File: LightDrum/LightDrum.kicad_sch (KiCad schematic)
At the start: 27 parts, among them J102 JTAG, Q101 RQ5A030AP, SW101 SW_SPDT, U101 STM32F103VEH6, U102 24LC04, Y101 8MHz, Y102 32.768KHz

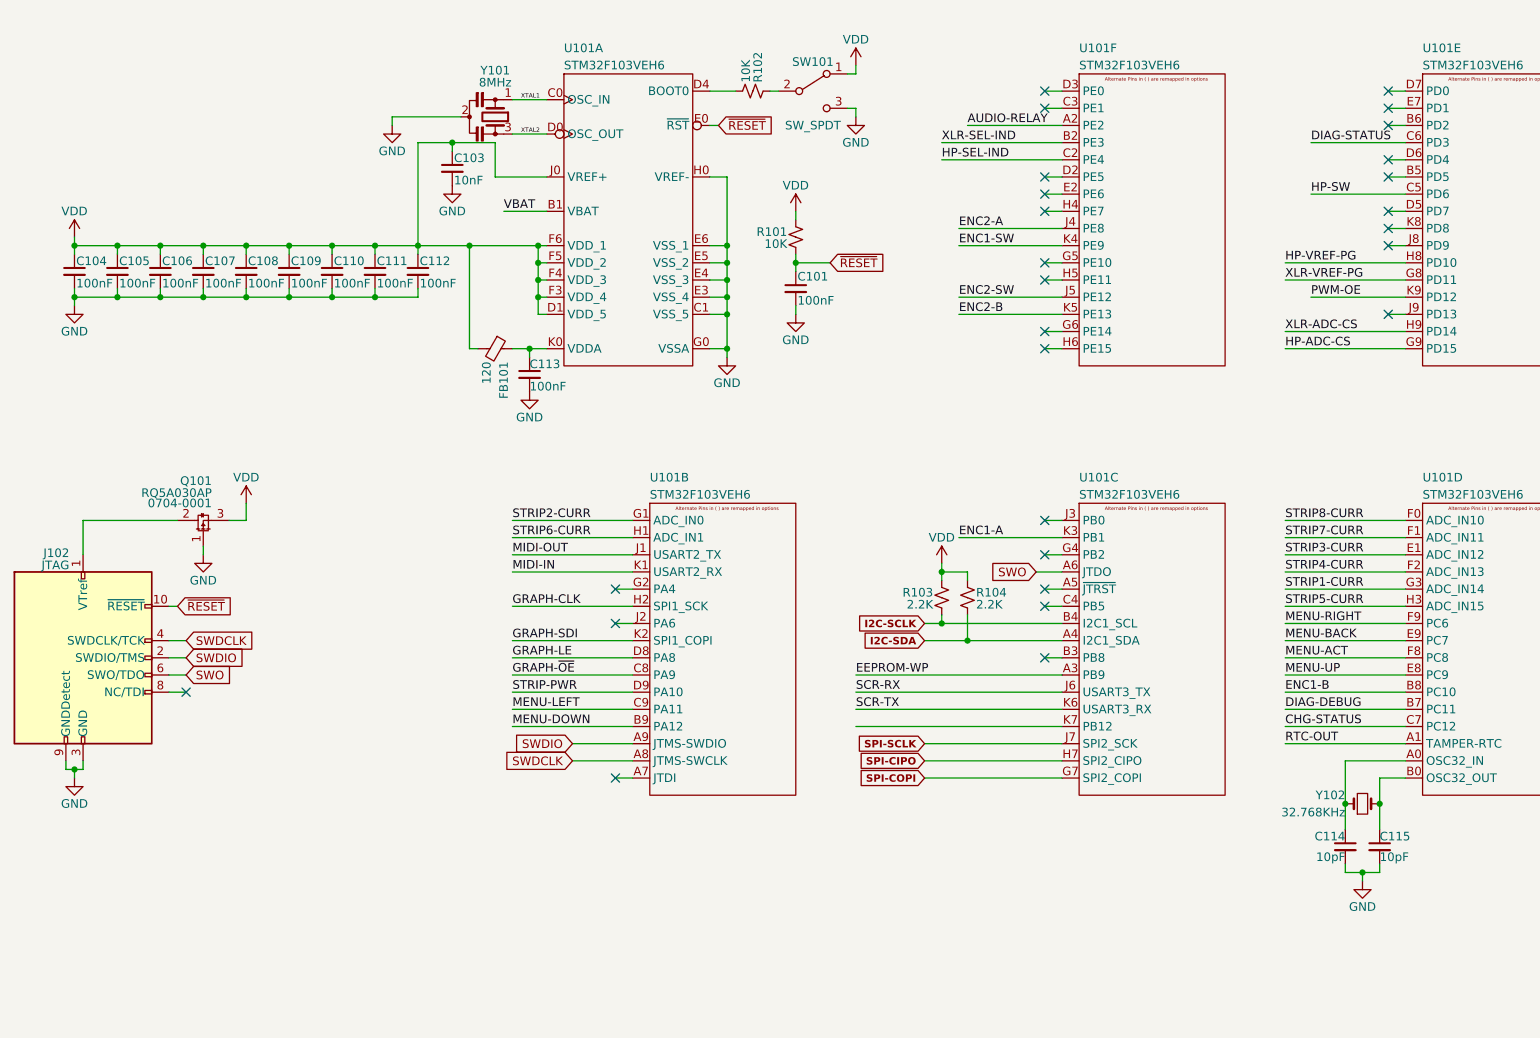
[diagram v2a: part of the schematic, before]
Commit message: Remove RTC and battery
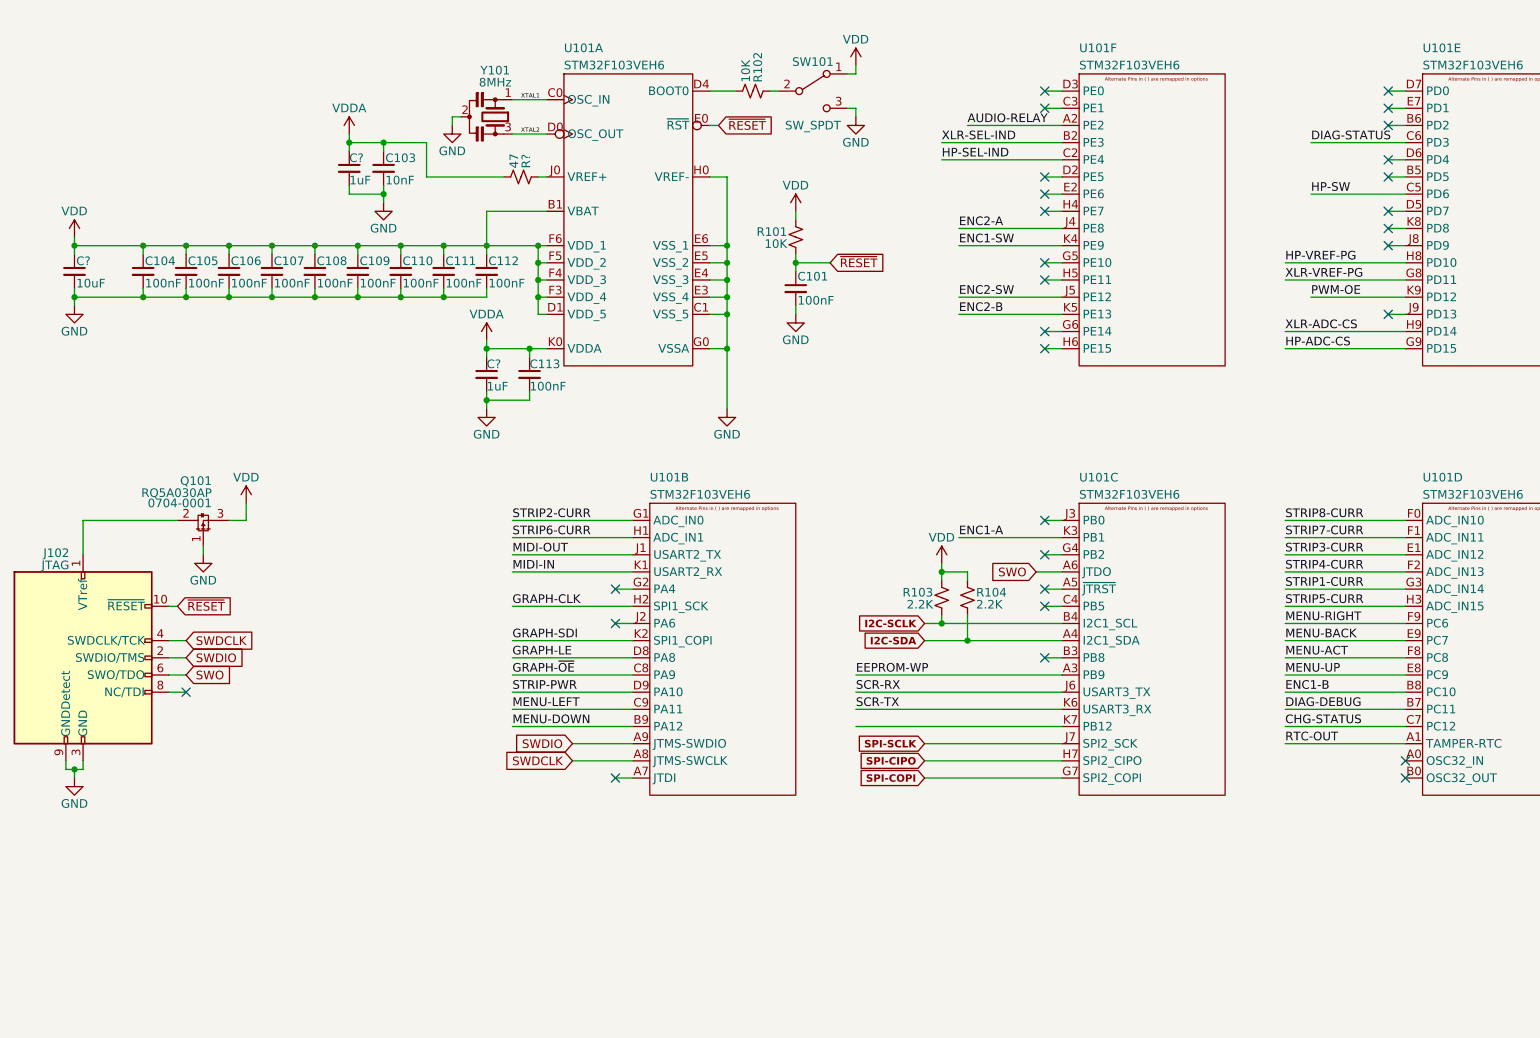
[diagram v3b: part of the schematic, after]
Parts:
- removed C114, C115: 10pF, Capacitor_SMD:C_0402_1005Metric, symbol Device:C_Small
- removed FB101: 120, Inductor_SMD:L_0603_1608Metric, symbol Device:FerriteBead_Small
- removed Y102: 32.768KHz, Crystal:Crystal_SMD_MicroCrystal_CC7V-T1A-2Pin_3.2x1.5mm, symbol Device:Crystal_Small
- added C? (x2): 1uF, Capacitor_SMD:C_0805_2012Metric, symbol Device:C_Small
- added C?: 10uF, Capacitor_SMD:C_1210_3225Metric, symbol Device:C_Small
- added R?: 47, Resistor_SMD:R_0402_1005Metric, symbol Device:R_Small_US
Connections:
- net GND: now also C?.2, C?.2, C?.2
- net VBAT: no longer U101.B1 (VBAT)
- net VDD: now also U101.B1 (VBAT), C?.1; no longer C103.1, U101.J0 (VREF+)
- net VDDA: now reaches C113.1, U101.K0 (VDDA)
- net VDDA: now also C103.1, C?.1, C?.1, R?.2
- new net: R?.1, U101.J0 (VREF+)
- no-connect marks 27 -> 29
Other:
- moved on the sheet: C103, C104, C105, C106, C107, C108, C109, C110, C111, C112

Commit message: Swap mcu again... (WIP)
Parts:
- removed C103: 10nF, Capacitor_SMD:C_0402_1005Metric, symbol Device:C_Small
- removed C104, C105, C106, C107, C108, C109, C110, C111, C112, C113: 100nF, Capacitor_SMD:C_0402_1005Metric, symbol Device:C_Small
- removed C? (x2): 1uF, Capacitor_SMD:C_0805_2012Metric, symbol Device:C_Small
- removed C?: 10uF, Capacitor_SMD:C_1210_3225Metric, symbol Device:C_Small
- removed R102: 10K, Resistor_SMD:R_0402_1005Metric, symbol Device:R_Small_US
- removed R?: 47, Resistor_SMD:R_0402_1005Metric, symbol Device:R_Small_US
- removed SW101: SW_SPDT, Daxxn_Switches:EG1218, symbol Switch:SW_SPDT
- removed U101: STM32F103VEH6, Daxxn_Packages:LFBGA-100_P0.8mm, symbol Daxxn_MicroControllers:STM32F103VEH6
- added C? (x2): 2.2uF, Capacitor_SMD:C_0805_2012Metric, symbol Device:C_Small
- added R? (x2): 10K, Resistor_SMD:R_0402_1005Metric, symbol Device:R_Small_US
- added STM101: STM32F446ZCH6, Daxxn_Packages:UFBGA144-7x7xOP6, symbol Daxxn_STMicros:STM32F446ZCH6
- added SW?: BOOT0, Daxxn_Switches:EG1218, symbol Switch:SW_SPDT
- added SW?: BOOT1, Daxxn_Switches:EG1218, symbol Switch:SW_SPDT
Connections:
- net GND: now also C?.2, C?.2, STM101.H5 (BYPASS-REG), SW?.3 (C), SW?.3 (C)
- net GRAPH-CLK: now also STM101.A3 (PE2)
- net GRAPH-SDI: now also STM101.B4 (PE6)
- net I2C-SCLK: now also STM101.C5 (PB8)
- net I2C-SDA: now also STM101.B5 (PB9)
- net MIDI-IN: now also STM101.A8 (PD6)
- net MIDI-OUT: now also STM101.B9 (PD5)
- net SCR-RX: now also STM101.D6 (PB7)
- net SCR-TX: now also STM101.C6 (PB6)
- net SPI-CIPO: now also STM101.H3 (PC2)
- net SPI-COPI: now also STM101.H2 (PC1)
- net SPI-SCLK: now also STM101.D9 (PD3)
- net STRIP1-CURR: now also STM101.J2 (PA0)
- net STRIP2-CURR: now also STM101.K2 (PA1)
- net STRIP3-CURR: now also STM101.L2 (PA2)
- net STRIP4-CURR: now also STM101.M2 (PA3)
- net STRIP5-CURR: now also STM101.J3 (PA4)
- net STRIP6-CURR: now also STM101.K3 (PA5)
- net STRIP7-CURR: now also STM101.L3 (PA6)
- net STRIP8-CURR: now also STM101.M3 (PA7)
- net SWDCLK: now also STM101.A11 (PA14/SWCLK)
- net SWDIO: now also STM101.A12 (PA13/SWDIO)
- net SWO: now also STM101.A7 (PB3/JTDO)
- net VDD: now also STM101.C2 (VBAT), STM101.E5 (PDR-ON), SW?.1 (A), SW?.1 (A)
- net XTAL1: now also STM101.D1 (OSC-IN)
- net XTAL2: now also STM101.E1 (OSC-OUT)
- net ~{RESET}: now also STM101.F1 (~{RESET})
- new net: R?.1, SW?.2 (B) (x2)
- new net: R?.2, STM101.D5 (BOOT0)
- new net: C?.1, STM101.H7 (VCAP1)
- new net: C?.1, STM101.G9 (VCAP2)
- new net BOOT1: R?.2, STM101.J5 (PB2/BOOT1)
- new net CAN-RX: STM101.C12 (PA11)
- new net CAN-TX: STM101.B12 (PA12)
- no-connect marks 29 -> 2
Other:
- sheet Interface Connectors ports: added I2C-SCLK, I2C-SDA, ~{RESET}; removed CHARGE-STATUS, VBAT
- moved on the sheet: C101, C102, J102, Q101, R101, R103, R104, U102, Y101

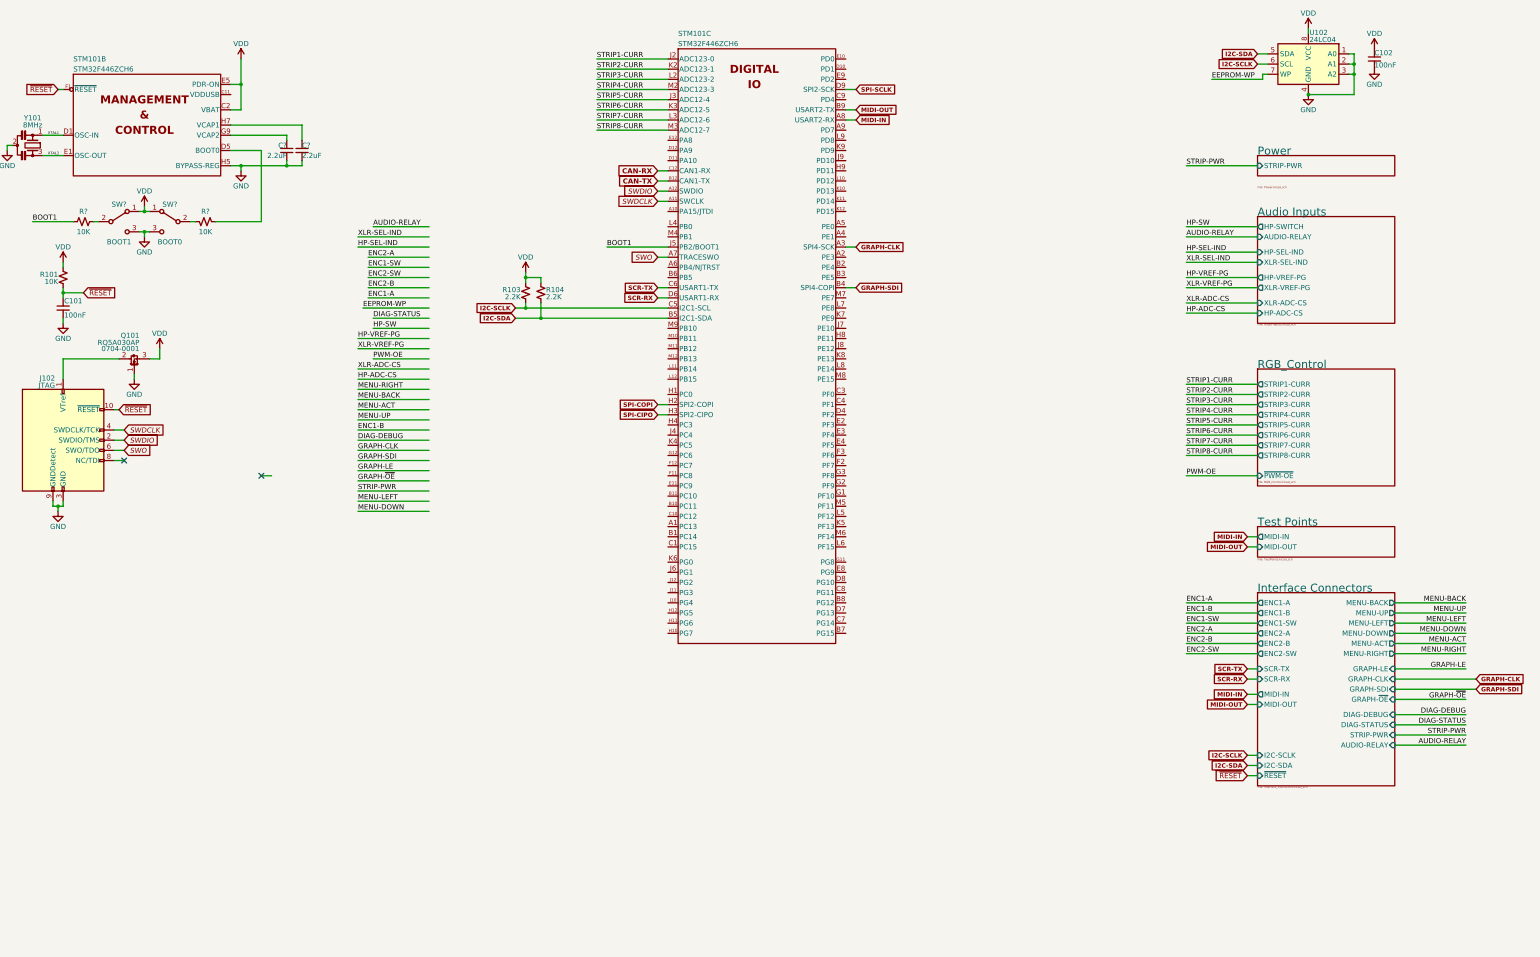
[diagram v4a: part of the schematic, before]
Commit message: Replace barrel jacks with proper DIN4 conn and more
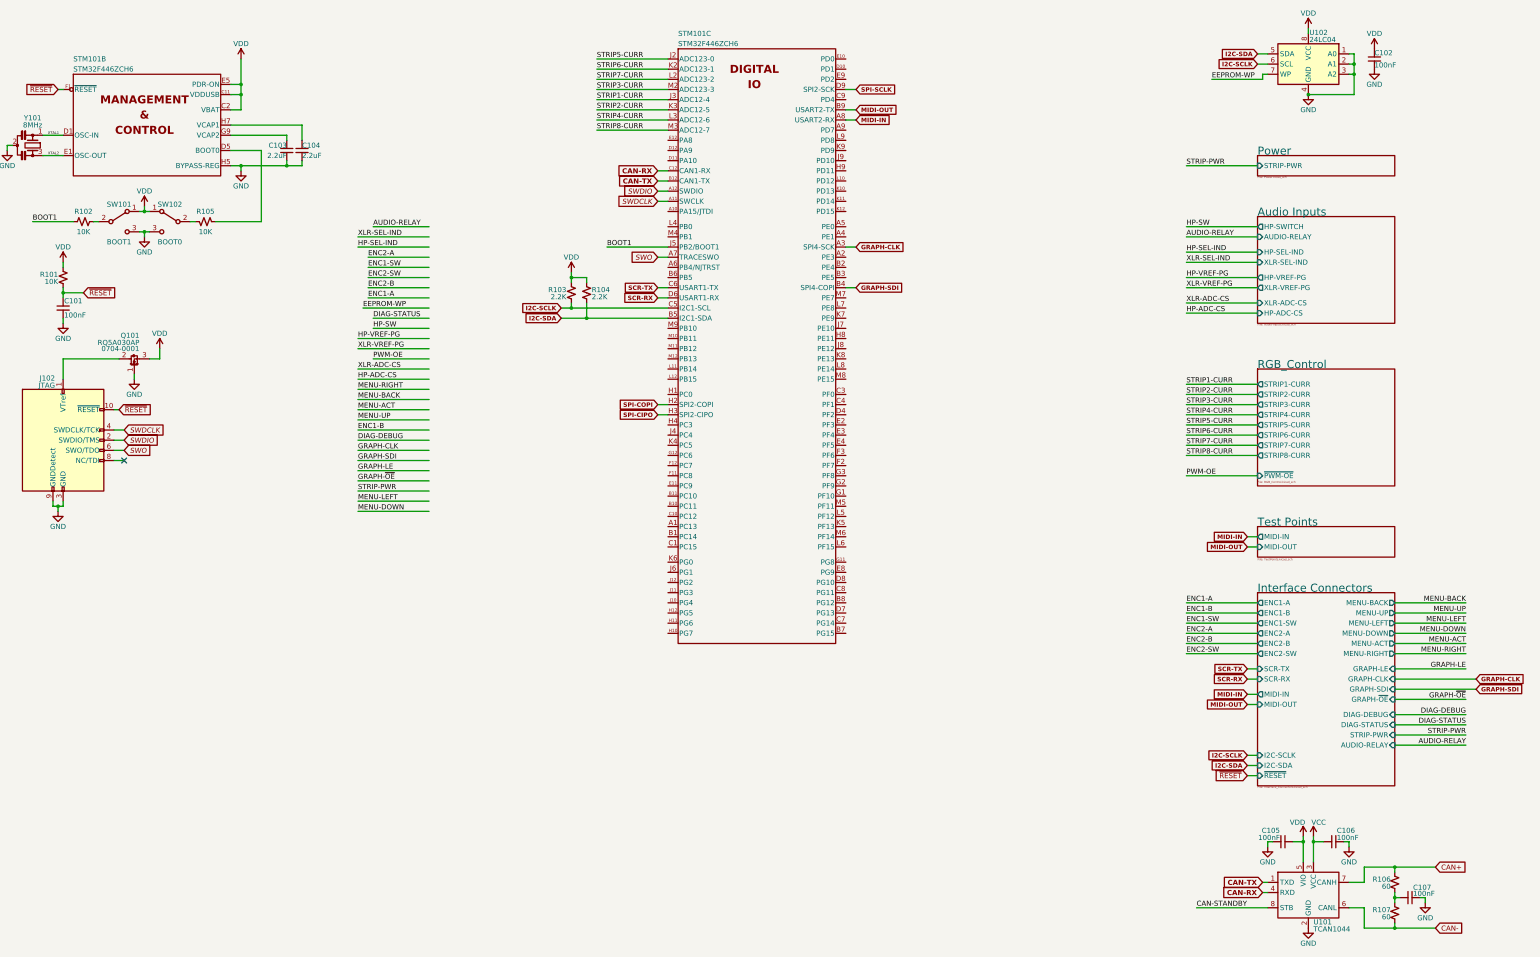
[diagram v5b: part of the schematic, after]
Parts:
- added C105, C106, C107: 100nF, Capacitor_SMD:C_0402_1005Metric, symbol Device:C_Small
- added R106, R107: 60, Resistor_SMD:R_0402_1005Metric, symbol Device:R_Small_US
- added U101: TCAN1044, Package_SO:SOIC-8_3.9x4.9mm_P1.27mm, symbol Daxxn_IC:TCAN1044
- C103, C104: renamed from C?; footprint Capacitor_SMD:C_0805_2012Metric -> Capacitor_SMD:C_0603_1608Metric
- SW101, SW102: renamed from SW?; footprint Daxxn_Switches:EG1218 -> Daxxn_Switches:PCM12SMTR
- gave numbers to parts that had none: 2
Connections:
- net CAN-RX: now also U101.4 (RXD)
- net CAN-TX: now also U101.1 (TXD)
- net GND: now also C105.1, C106.1, C107.1, U101.2 (GND)
- net STRIP1-CURR: now also STM101.J3 (PA4); no longer STM101.J2 (PA0)
- net STRIP2-CURR: now also STM101.K3 (PA5); no longer STM101.K2 (PA1)
- net STRIP3-CURR: now also STM101.M2 (PA3); no longer STM101.L2 (PA2)
- net STRIP4-CURR: now also STM101.L3 (PA6); no longer STM101.M2 (PA3)
- net STRIP5-CURR: now also STM101.J2 (PA0); no longer STM101.J3 (PA4)
- net STRIP6-CURR: now also STM101.K2 (PA1); no longer STM101.K3 (PA5)
- net STRIP7-CURR: now also STM101.L2 (PA2); no longer STM101.L3 (PA6)
- net VDD: now also STM101.C11 (VDDUSB), C105.2, U101.5 (VIO)
- new net: C107.2, R106.2, R107.1
- new net CAN+: R106.1, U101.7 (CANH)
- new net CAN-: R107.2, U101.6 (CANL)
- new net CAN-STANDBY: U101.8 (STB)
- new net VCC: C106.2, U101.3 (VCC)
- no-connect marks 2 -> 1
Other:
- moved on the sheet: R103, R104

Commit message: Lock REV8 Layout and send to PCB MNF
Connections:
- net AUDIO-RELAY: now also STM101.C4 (PF1)
- net DIAG-DEBUG: now also STM101.L11 (PB14)
- net DIAG-STATUS: now also STM101.M11 (PB12)
- net EEPROM-WP: now also STM101.B7 (PG15)
- net ENC1-A: now also STM101.M4 (PB1)
- net ENC1-B: now also STM101.L10 (PD12)
- net ENC1-SW: now also STM101.L4 (PB0)
- net ENC2-A: now also STM101.M5 (PF11)
- net ENC2-B: now also STM101.L5 (PF12)
- net ENC2-SW: now also STM101.M6 (PF14)
- net GRAPH-LE: now also STM101.L8 (PE14)
- net GRAPH-~{OE}: now also STM101.L9 (PD8)
- net HP-ADC-CS: now also STM101.K12 (PD15)
- net HP-SEL-IND: now also STM101.A5 (PE0)
- net HP-SW: now also STM101.M12 (PB13)
- net MENU-ACT: now also STM101.M7 (PE7)
- net MENU-BACK: now also STM101.L7 (PE8)
- net MENU-DOWN: now also STM101.M10 (PB11)
- net MENU-LEFT: now also STM101.M9 (PB10)
- net MENU-RIGHT: now also STM101.L6 (PF15)
- net MENU-UP: now also STM101.M8 (PE15)
- net PWM-OE: now also STM101.D12 (PA9)
- net STRIP-PWR: now also STM101.H12 (PG5)
- net VCC: now also U101.5 (VIO); no longer U101.3 (VCC)
- net VDD: now also U101.3 (VCC); no longer U101.5 (VIO)
- net XLR-ADC-CS: now also STM101.J12 (PG2)
- net XLR-SEL-IND: now also STM101.A4 (PE1)
- net XLR-VREF-IRQ: now reaches STM101.J10 (PG4)
- net HP-VREF-IRQ: now reaches STM101.J9 (PD10)
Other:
- sheet Audio Inputs ports: added HP-ADC-IRQ, XLR-ADC-IRQ; removed HP-VREF-PG, XLR-VREF-PG
